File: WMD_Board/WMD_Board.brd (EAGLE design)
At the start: 65 x 45 mm, 45 parts, among them J1 EMPCB.SMAFSTJ.B.HT, U1 STM32L053C8T6, U2 BSS138, U3 RFM69HCW, U4 BSS138, Y2 ABS06-107-32.768KHZ-T

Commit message: More Schematic Work
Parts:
- added C19, C20, C21: 0.1uF, SparkFun-Capacitors:0603
- added R16, R17: 4.7k, SparkFun-Resistors:0603
- added U5: M24512-DRMN8TP/K, M24512_EEPROM:SOIC127P600X175-8N
- added U6: TPS72218DBVR, TPS72218DBVR_LDO:DBV5
- U$20: value TS_DR_10 -> TS_DR_6; device TST_Connnector:TST_DR_10 -> TST_Connnector:TST_DR_6
- moved Y2 114.1 mm to (57.5, 10.0)
- moved U2 109.5 mm to (46.9, 7.11), turned to 90 degrees
- moved U3 101.7 mm to (54.4, 28.4), turned to 90 degrees
- moved U$10 101.7 mm to (55.9, 12.6)
- moved J1 96.1 mm to (61.3, 42.3), turned to 180 degrees
- moved JP1 82.9 mm to (61.3, 38.9)
- moved U4 75.5 mm to (46.9, 11.7), turned to 90 degrees
- moved SV2 58.5 mm to (29.8, 1.78)
- moved U1 50.1 mm to (25.9, 30.0), turned to 270 degrees
- moved U$20 15.1 mm to (0.13, 0.13)
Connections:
- net CS renamed LORA_CS
- net RST renamed LORA_RESET
- net SPI1_MISO renamed LORA_MISO
- net SPI1_MOSI renamed LORA_MOSI
- net SPI1_SCK renamed LORA_SCK
- removed net BTN_1_1: R7.1, R8.2, U$20.11
- removed net BTN_2_1: R10.1, R11.2, U$20.12
- removed net BTN_3_1: R12.1, R13.2, U$20.13
- removed net BTN_4_1: R14.1, R15.2, U$20.14
- removed net DIO5: U3.15P
- removed net GPS_RX: U1.22
- removed net GPS_TX: U1.21
- removed net MFIO: U$10.MFIO@1, U$10.MFIO@2
- removed net N$2: R2.2, U1.25
- removed net RSTN: C14.1, U$10.RSTN
- new net BTN1_OUT: R7.1, R8.2, U$20.1
- new net BTN2_OUT: R10.1, R11.2, U$20.2
- new net BTN3_OUT: R12.1, R13.2, U$20.7
- new net BTN4_OUT: R14.1, R15.2, U$20.8
- new net HR_MFIO: U$10.MFIO@1, U$10.MFIO@2, U1.40
- new net HR_RESET: C14.1, U$10.RSTN, U1.41
- new net LORA_DIO5: U1.19, U3.15P
- new net N$1: R2.2, U1.39
- new net OLED_CS: U$20.3, U1.25
- new net OLED_DC: U$20.5, U1.27
- new net OLED_MOSI: U$20.6, U1.28
- new net OLED_RESET: U$20.12, U1.29
- new net OLED_SCK: U$20.4, U1.26
- new net WC_EEPROM: U1.46, U5.7
- net 1.8V: now also C20.1, U6.5
- net 3.3V: now also C19.1, C21.1, R16.1, R17.1, U$20.11, U5.8, U6.1, U6.3
- net BTN1: now also U1.10
- net BTN2: now also U1.11
- net BTN3: now also U1.12
- net BTN4: now also U1.13
- net DIO0: no longer U1.19
- net GND: now also C19.2, C20.2, C21.2, U$20.10, U$20.9, U5.1, U5.2, U5.3, U5.4, U6.2; no longer U$20.1, U$20.2, U$20.3, U$20.4
- net SCL_EEPROM: now also R17.2, U1.21, U5.6; no longer U1.26
- net SDA_EEPROM: now also R16.2, U1.22, U5.5; no longer U1.27

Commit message: stuff
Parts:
- moved JP1 12.1 mm to (49.3, 39.1)
- moved J1 11.9 mm to (49.4, 42.5), flipped to the bottom
- moved U3 1.20 mm to (55.5, 28.8), flipped to the bottom
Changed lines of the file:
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@@
 <attribute name="PROD_ID" value="CAP-00810" x="-54.61" y="54.61" size="1.778" layer="27" display="off"/>
 </element>
-<element name="J1" library="EMPCB.SMAFSTJ.B.HT" package="TAOGLAS_EMPCB.SMAFSTJ.B.HT" value="EMPCB.SMAFSTJ.B.HT" x="61.341" y="42.291" rot="R180">
-<attribute name="DESCRIPTION" value=" SMA Connector Jack, Female Socket 50Ohm Board Edge, End Launch Solder " x="61.341" y="42.291" size="1.778" layer="27" rot="R180" display="off"/>
-<attribute name="DIGI-KEY_PART_NUMBER" value="931-1175-ND" x="61.341" y="42.291" size="1.778" layer="27" rot="R180" display="off"/>
-<attribute name="DIGI-KEY_PURCHASE_URL" value="https://www.digikey.com/product-detail/en/taoglas-limited/EMPCB.SMAFSTJ.B.HT/931-1175-ND/3522337?utm_source=snapeda&amp;utm_medium=aggregator&amp;utm_campaign=symbol" x="61.341" y="42.291" size="1.778" layer="27" rot="R180" display="off"/>
-<attribute name="MF" value="Taoglas Limited" x="61.341" y="42.291" size="1.778" layer="27" rot="R180" display="off"/>
-<attribute name="MP" value="EMPCB.SMAFSTJ.B.HT" x="61.341" y="42.291" size="1.778" layer="27" rot="R180" display="off"/>
-<attribute name="PACKAGE" value="None" x="61.341" y="42.291" size="1.778" layer="27" rot="R180" display="off"/>
-</element>
-<element name="JP1" library="microbuilder" package="1X01_ROUND" value="" x="61.341" y="38.862"/>
+<element name="J1" library="EMPCB.SMAFSTJ.B.HT" package="TAOGLAS_EMPCB.SMAFSTJ.B.HT" value="EMPCB.SMAFSTJ.B.HT" x="49.403" y="42.545" rot="MR180">
+<attribute name="DESCRIPTION" value=" SMA Connector Jack, Female Socket 50Ohm Board Edge, End Launch Solder " x="49.403" y="42.545" size="1.778" layer="28" rot="MR180" display="off"/>
+<attribute name="DIGI-KEY_PART_NUMBER" value="931-1175-ND" x="49.403" y="42.545" size="1.778" layer="28" rot="MR180" display="off"/>
+<attribute name="DIGI-KEY_PURCHASE_URL" value="https://www.digikey.com/product-detail/en/taoglas-limited/EMPCB.SMAFSTJ.B.HT/931-1175-ND/3522337?utm_source=snapeda&amp;utm_medium=aggregator&amp;utm_campaign=symbol" x="49.403" y="42.545" size="1.778" layer="28" rot="MR180" display="off"/>
+<attribute name="MF" value="Taoglas Limited" x="49.403" y="42.545" size="1.778" layer="28" rot="MR180" display="off"/>
+<attribute name="MP" value="EMPCB.SMAFSTJ.B.HT" x="49.403" y="42.545" size="1.778" layer="28" rot="MR180" display="off"/>
+<attribute name="PACKAGE" value="None" x="49.403" y="42.545" size="1.778" layer="28" rot="MR180" display="off"/>
+</element>
+<element name="JP1" library="microbuilder" package="1X01_ROUND" value="" x="49.276" y="39.116"/>
 <element name="LED1" library="led" library_urn="urn:adsk.eagle:library:259" package="CHIP-LED0805" package3d_urn="urn:adsk.eagle:package:15818/2" value="" x="-31.75" y="48.26">
 <attribute name="POPULARITY" value="68" x="-31.75" y="48.26" size="1.778" layer="27" display="off"/>
@@
 <attribute name="VENDOR" value="Fairchild Semiconductor" x="46.863" y="7.112" size="1.778" layer="27" rot="R90" display="off"/>
 </element>
-<element name="U3" library="microbuilder" package="RFMHCW_SMT" value="RFM69HCW" x="54.356" y="28.448" rot="R90"/>
+<element name="U3" library="microbuilder" package="RFMHCW_SMT" value="RFM69HCW" x="55.499" y="28.829" rot="MR90"/>
 <element name="U4" library="BSS138" package="SOT-23-3L" value="BSS138" x="46.863" y="11.684" rot="R90">
 <attribute name="MANUFACTURER_PART_NUMBER" value="BSS138" x="46.863" y="11.684" size="1.778" layer="27" rot="R90" display="off"/>
@@
 <contactref element="C21" pad="2"/>
 <contactref element="U6" pad="2"/>
-<wire x1="64.111" y1="42.291" x2="64.111" y2="42.291" width="0" layer="19" extent="1-16"/>
-<wire x1="58.571" y1="42.291" x2="64.111" y2="42.291" width="0" layer="19" extent="1-1"/>
-<wire x1="58.571" y1="42.291" x2="58.571" y2="42.291" width="0" layer="19" extent="1-16"/>
-<wire x1="59.356" y1="36.548" x2="58.571" y2="42.291" width="0" layer="19" extent="1-1"/>
-<wire x1="61.356" y1="20.348" x2="59.356" y2="36.548" width="0" layer="19" extent="1-1"/>
-<wire x1="58.18" y1="14.173" x2="61.356" y2="20.348" width="0" layer="19" extent="1-1"/>
+<wire x1="52.173" y1="42.545" x2="46.633" y2="42.545" width="0" layer="19" extent="1-1"/>
+<wire x1="50.499" y1="36.929" x2="52.173" y2="42.545" width="0" layer="19" extent="1-1"/>
+<wire x1="48.499" y1="20.729" x2="50.499" y2="36.929" width="0" layer="19" extent="1-1"/>
+<wire x1="58.18" y1="14.173" x2="48.499" y2="20.729" width="0" layer="19" extent="1-1"/>
 <wire x1="58.03" y1="12.723" x2="58.18" y2="14.173" width="0" layer="19" extent="1-1"/>
 <wire x1="56.83" y1="12.623" x2="58.03" y2="12.723" width="0" layer="19" extent="1-1"/>
 <wire x1="56.58" y1="12.973" x2="56.83" y2="12.623" width="0" layer="19" extent="1-1"/>
-<wire x1="47.356" y1="20.348" x2="56.58" y2="12.973" width="0" layer="19" extent="1-1"/>
-<wire x1="28.158" y1="25.792" x2="47.356" y2="20.348" width="0" layer="19" extent="1-1"/>
+<wire x1="62.499" y1="20.729" x2="56.58" y2="12.973" width="0" layer="19" extent="1-1"/>
+<wire x1="28.158" y1="25.792" x2="62.499" y2="20.729" width="0" layer="19" extent="1-1"/>
 <wire x1="30.088" y1="32.222" x2="28.158" y2="25.792" width="0" layer="19" extent="1-1"/>
 <wire x1="25.158" y1="34.152" x2="30.088" y2="32.222" width="0" layer="19" extent="1-1"/>
@@
 <contactref element="U6" pad="1"/>
 <contactref element="C21" pad="1"/>
-<wire x1="30.088" y1="32.722" x2="53.356" y2="36.548" width="0" layer="19" extent="1-1"/>
+<wire x1="30.088" y1="32.722" x2="56.499" y2="36.929" width="0" layer="19" extent="1-1"/>
 <wire x1="24.658" y1="34.152" x2="30.088" y2="32.722" width="0" layer="19" extent="1-1"/>
 <wire x1="28.658" y1="25.792" x2="30.088" y2="32.722" width="0" layer="19" extent="1-1"/>
@@
 <contactref element="JP1" pad="1"/>
 <contactref element="J1" pad="1"/>
-<wire x1="61.341" y1="38.862" x2="61.341" y2="42.291" width="0" layer="19" extent="1-1"/>
-<wire x1="61.356" y1="36.548" x2="61.341" y2="38.862" width="0" layer="19" extent="1-1"/>
+<wire x1="49.276" y1="39.116" x2="49.403" y2="42.545" width="0" layer="19" extent="1-1"/>
+<wire x1="48.499" y1="36.929" x2="49.276" y2="39.116" width="0" layer="19" extent="1-1"/>
 </signal>
 <signal name="DIO3">
@@
 <contactref element="U3" pad="10P"/>
 <contactref element="U1" pad="16"/>
-<wire x1="21.728" y1="31.222" x2="49.356" y2="20.348" width="0" layer="19" extent="1-1"/>
+<wire x1="21.728" y1="31.222" x2="60.499" y2="20.729" width="0" layer="19" extent="1-1"/>
 </signal>
 <signal name="LORA_MOSI">
 <contactref element="U3" pad="11P"/>
 <contactref element="U1" pad="17"/>
-<wire x1="21.728" y1="30.722" x2="51.356" y2="20.348" width="0" layer="19" extent="1-1"/>
+<wire x1="21.728" y1="30.722" x2="58.499" y2="20.729" width="0" layer="19" extent="1-1"/>
 </signal>
 <signal name="LORA_SCK">
 <contactref element="U3" pad="12P"/>
 <contactref element="U1" pad="15"/>
-<wire x1="21.728" y1="31.722" x2="53.356" y2="20.348" width="0" layer="19" extent="1-1"/>
+<wire x1="21.728" y1="31.722" x2="56.499" y2="20.729" width="0" layer="19" extent="1-1"/>
 </signal>
 <signal name="LORA_CS">
 <contactref element="U3" pad="13P"/>
 <contactref element="U1" pad="14"/>
-<wire x1="21.728" y1="32.222" x2="55.356" y2="20.348" width="0" layer="19" extent="1-1"/>
+<wire x1="21.728" y1="32.222" x2="54.499" y2="20.729" width="0" layer="19" extent="1-1"/>
 </signal>
 <signal name="OLED_MOSI">
@@
 <contactref element="U1" pad="18"/>
 <contactref element="U3" pad="14P"/>
-<wire x1="21.728" y1="30.222" x2="57.356" y2="20.348" width="0" layer="19" extent="1-1"/>
+<wire x1="21.728" y1="30.222" x2="52.499" y2="20.729" width="0" layer="19" extent="1-1"/>
 </signal>
 <signal name="LORA_DIO5">
 <contactref element="U3" pad="15P"/>
 <contactref element="U1" pad="19"/>
-<wire x1="21.728" y1="29.722" x2="59.356" y2="20.348" width="0" layer="19" extent="1-1"/>
+<wire x1="21.728" y1="29.722" x2="50.499" y2="20.729" width="0" layer="19" extent="1-1"/>
 </signal>
 <signal name="N$1">

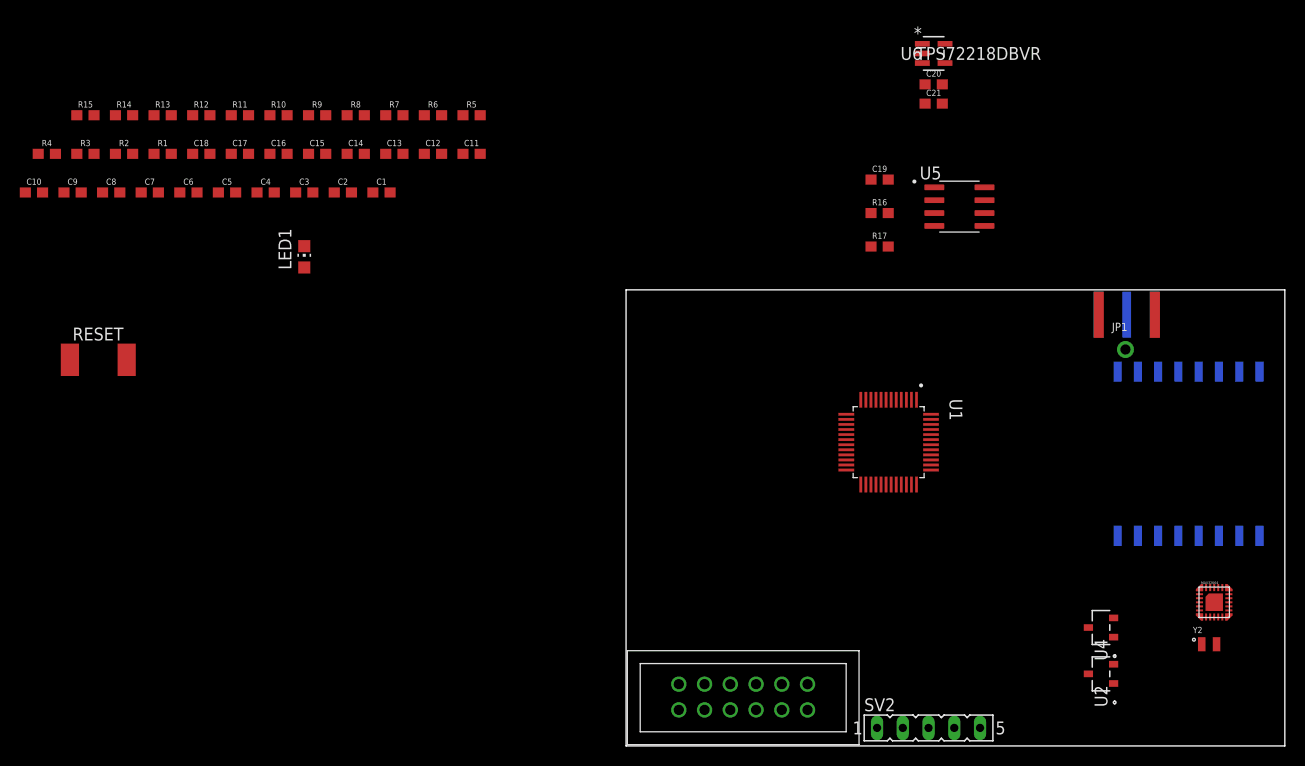
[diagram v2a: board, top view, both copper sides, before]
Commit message: added gps module
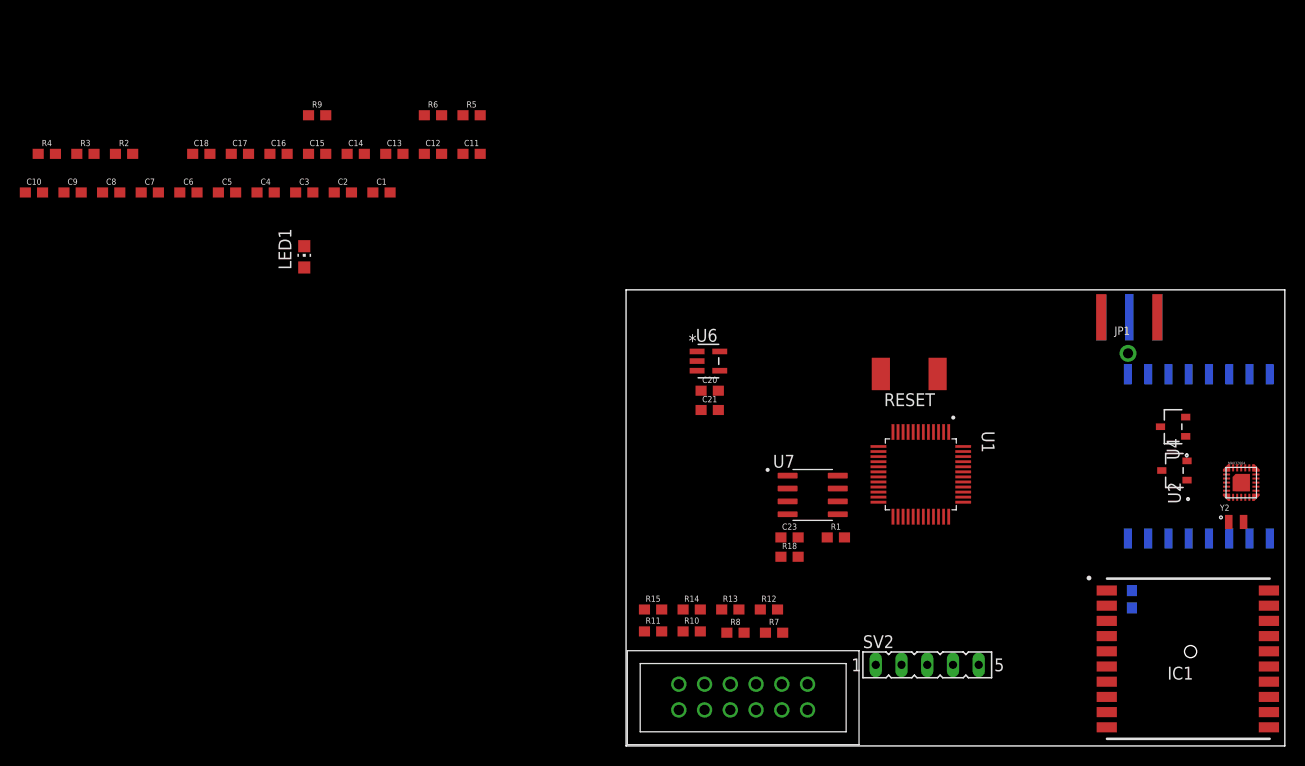
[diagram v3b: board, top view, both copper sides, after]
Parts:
- removed C19: 0.1uF, SparkFun-Capacitors:0603
- removed R16, R17: 4.7k, SparkFun-Resistors:0603
- removed U5: M24512-DRMN8TP/K, M24512_EEPROM:SOIC127P600X175-8N
- added C22, C23: 0.1uF, SparkFun-Capacitors:0603
- added IC1: FGPMMOPA6H, FGPMMOPA6H:FGPMMOPA6H
- added R18: 4.7k, SparkFun-Resistors:0603
- added U7: M24512-DRMN8TP/K, M24512_EEPROM:SOIC127P600X175-8N
- C17: value 4.7uF -> 0.1uF
- R1: value 1k -> 4.7k
- moved RESET 80.0 mm to (27.9, 36.7), turned to 180 degrees
- moved R1 76.4 mm to (20.7, 20.6)
- moved R12 74.3 mm to (14.1, 13.5)
- moved R13 74.3 mm to (10.3, 13.5)
- moved R14 74.3 mm to (6.48, 13.5)
- moved R15 74.3 mm to (2.67, 13.5)
- moved R11 65.2 mm to (2.67, 11.3)
- moved R10 65.2 mm to (6.48, 11.3)
- moved R7 63.3 mm to (14.6, 11.2)
- moved R8 63.3 mm to (10.8, 11.2)
- moved U6 37.6 mm to (8.13, 38.0)
- moved C20 37.4 mm to (8.26, 35.1)
- moved C21 37.4 mm to (8.26, 33.1)
- moved U2 21.3 mm to (54.1, 27.2)
- moved U4 21.0 mm to (54.0, 31.5)
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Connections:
- new net GPS_NRST: IC1.2, U1.32
- new net GPS_RX: IC1.9, U1.31
- new net GPS_TX: IC1.10, U1.30
- net 3.3V: now also C22.1, C23.1, IC1.1, R1.1, R18.1, U7.8; no longer C19.1, R1.2, R16.1, R17.1, U5.8
- net GND: now also C22.2, C23.2, IC1.12, IC1.19, IC1.3, IC1.8, U7.1, U7.2, U7.3, U7.4; no longer C19.2, U5.1, U5.2, U5.3, U5.4
- net NRST: no longer R1.1
- net SCL_EEPROM: now also R18.2, U7.6; no longer R17.2, U5.6
- net SDA_EEPROM: now also R1.2, U7.5; no longer R16.2, U5.5
- net WC_EEPROM: now also U7.7; no longer U5.7

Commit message: Added lots of schematic stuff
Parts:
- removed C2: 0.1uF, SparkFun-Capacitors:0603
- added C19, C24, C25: 10uF, SparkFun-Capacitors:0603
- added C26: 0.1uF, SparkFun-Capacitors:0603
- added L1: 2.2uH/NRH2412T2R2MNGH, microbuilder:INDUCTOR_TAIYOYUDEN_NRH2412T
- added Q1: SI2323DS-T1-E3, SI2323DS-T1-E3:SOT23
- added R16: 100, SparkFun-Resistors:0603
- added U$22: TPS63001, TPS63001:TPS63001
- R7, R8: value 10k -> 100k
- moved R7 107.5 mm to (-62.5, -63.8)
- moved R8 107.2 mm to (-62.5, -67.1)
- moved C20 101.2 mm to (-62.5, -37.3)
- moved U6 99.3 mm to (-60.3, -33.9)
- moved C21 97.5 mm to (-59.2, -37.3)
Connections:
- removed net BTN1: C2.1, R8.1, U1.10
- removed net BTN1_OUT: R7.1, R8.2, U$20.1
- removed net BTN_1_2: C2.2
- new net BTN_POWER_OUT: U$20.1
- new net N$2: L1.1, U$22.4
- new net N$3: L1.2, U$22.2
- new net N$4: R7.2, R8.1, U1.10
- new net N$7: C26.1, R16.1, U$22.6, U$22.7, U$22.8
- new net VIN_BATTERY: Q1.3
- new net VIN_BB: C25.1, R16.2, U$22.5
- new net V_BAT_MEASURE: R7.1
- net 3.3V: now also C19.1, C24.1, U$22.1, U$22.10; no longer R7.2
- net GND: now also C19.2, C24.2, C25.2, C26.2, Q1.1, R8.2, U$22.11, U$22.3, U$22.9, U1.44
